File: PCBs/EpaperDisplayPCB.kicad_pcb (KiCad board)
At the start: 2 copper layers, 84 x 40.1 mm, 21 parts, among them J1 Conn_01x08, J2 Conn_01x12_FPC_0.5mm, Q1 AO3404A, U1 ePaper-2.1

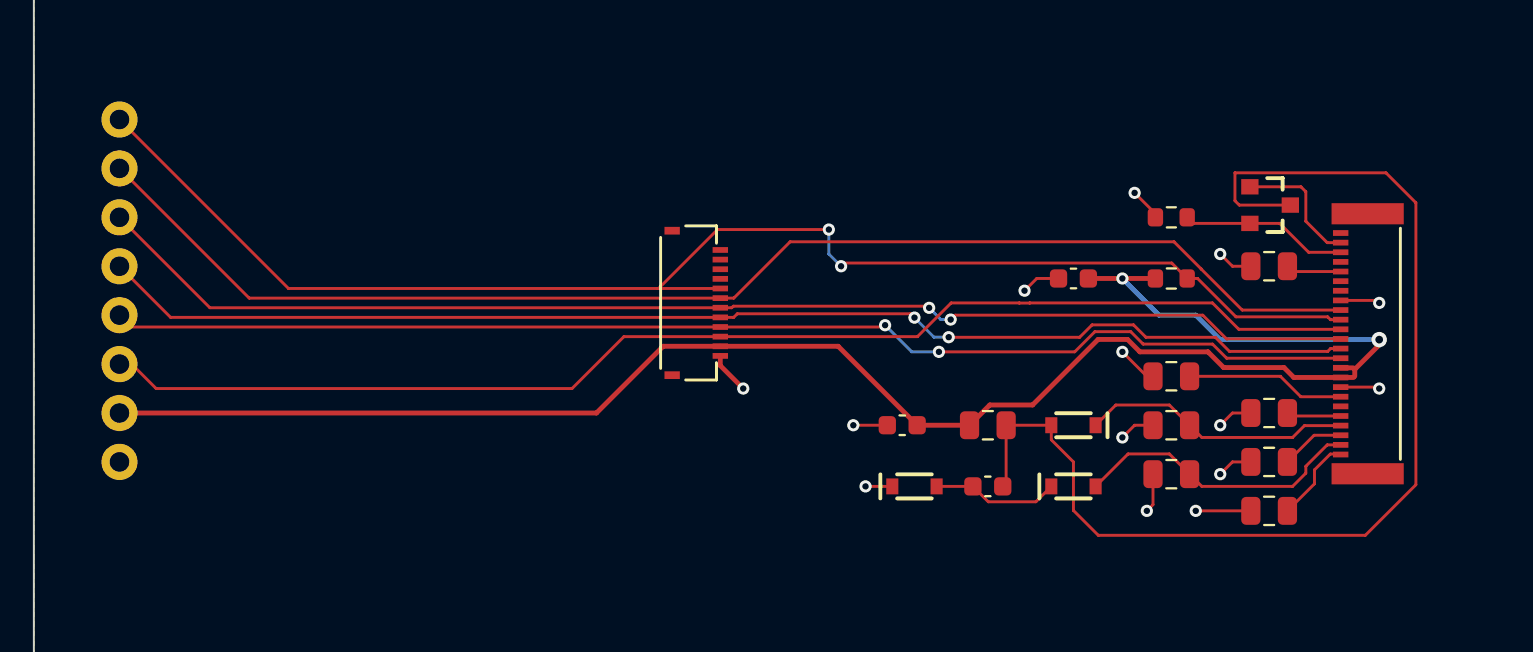
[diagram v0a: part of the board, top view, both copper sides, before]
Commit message: Updates
Fixing connections between epaper display board and main board pcbs
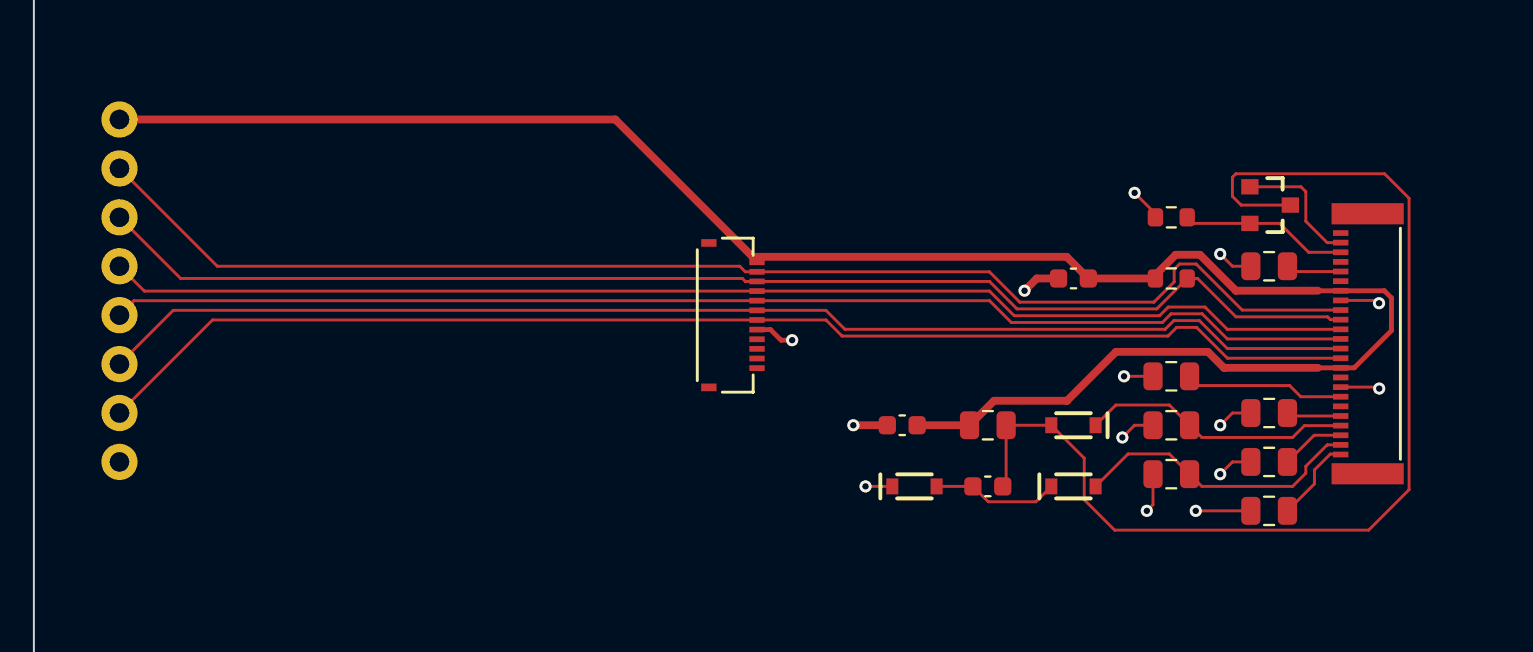
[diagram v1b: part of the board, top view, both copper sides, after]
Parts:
- removed the J2 at (152.6, 87.5)
- added J1: Conn_01x12_FPC_0.5mm, SparkFun-Connector:FPC_12_0.5MM, F.Cu at (154.6, 88.2)
- renumbered J1 to J2
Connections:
- J2 pad 1: ~{RST} -> +3.3V
- J2 pad 3: ~{CS} -> ~{RST}
- J2 pad 4: SCLK -> D/~{C}
- J2 pad 5: SDIO -> ~{CS}
- J2 pad 6: D/~{C} -> SCLK
- J2 pad 7: +3.3V -> SDIO
- U1 pad 16: +3.3V -> unconnected-(U1-NC-Pad16)
- U1 pad 7: unconnected-(U1-NC-Pad7) -> +3.3V
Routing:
- net +3.3V: track 91.3 -> 100.4 mm, vias 2 -> 0
- net ~{RST}: track 74.4 -> 66.9 mm, vias 2 -> 0
- net ~{CS}: track 66.3 -> 64.9 mm, vias 2 -> 0
- net Net-(Q1-D): track 59.0 -> 57.6 mm
- net SDIO: track 65.3 -> 66.6 mm, vias 2 -> 0
- net D/~{C}: track 66.3 -> 65.1 mm
- net GND: track 27.6 -> 26.8 mm
- net SCLK: track 66.0 -> 65.8 mm, vias 2 -> 0

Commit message: Updates
Screen PCB updates
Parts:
- added FID1: Fiducial_0.5mm, SparkFun-Aesthetic:Fiducial_0.5mm_Mask1mm, F.Cu at (122.8, 104.1)
- added FID2: Fiducial_0.5mm, SparkFun-Aesthetic:Fiducial_0.5mm_Mask1mm, F.Cu at (195.2, 72.9)
- added FID3: Fiducial_0.5mm, SparkFun-Aesthetic:Fiducial_0.5mm_Mask1mm, B.Cu at (195.2, 103.4)
- added FID4: Fiducial_0.5mm, SparkFun-Aesthetic:Fiducial_0.5mm_Mask1mm, B.Cu at (122.2, 71.0)
- added G***: LOGO, SparkFun-Aesthetic:SparkFun_Logo_NoFlame_12.5mm, F.Cu at (143.8, 100.2)
- added Ref**: Val**, SparkFun-Aesthetic:OSHW_Logo_6mm, F.Cu at (133.6, 100.2)
- added kibuzzard-65B1FFD4: G***, kibuzzard-65B1FFD4, F.Cu at (120.1, 78.1)
- added kibuzzard-65B1FFE5: G***, kibuzzard-65B1FFE5, F.Cu at (120.3, 80.6)
- added kibuzzard-65B20022: G***, kibuzzard-65B20022, F.Cu at (120.3, 83.1)
- added kibuzzard-65B20037: G***, kibuzzard-65B20037, F.Cu at (120.3, 85.6)
- added kibuzzard-65B20040: G***, kibuzzard-65B20040, F.Cu at (120.3, 88.2)
- added kibuzzard-65B2004E: G***, kibuzzard-65B2004E, F.Cu at (120.3, 90.7)
- added kibuzzard-65B2005D: G***, kibuzzard-65B2005D, F.Cu at (120.3, 93.3)
- added kibuzzard-65B2006B: G***, kibuzzard-65B2006B, F.Cu at (120.3, 95.8)
- added kibuzzard-65B200B7: G***, kibuzzard-65B200B7, F.Cu at (195.2, 97.1)
- added kibuzzard-65B200B7: G***, kibuzzard-65B200B7, F.Cu at (195.2, 82.5)
- added kibuzzard-65B200D7: G***, kibuzzard-65B200D7, F.Cu at (154.6, 93.3)
- added kibuzzard-65B20298: G***, kibuzzard-65B20298, F.Cu at (161.5, 74.2)
- U1: value ePaper-2.1 -> ePaper-2.13

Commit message: Updated Epaper Display
Updated Epaper Display with new schematic symbol and placed the correct footprint onto the PCB
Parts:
- U1: value ePaper-2.13 -> ePaper-2.66; footprint SparkFun-Display:ePaper-2.13 -> SparkFun-Display:ePaper-2.66

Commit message: epaper update
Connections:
- U1 pad 16: unconnected-(U1-NC-Pad16) -> +3.3V
- U1 pad 7: +3.3V -> unconnected-(U1-NC-Pad7)
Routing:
- net +3.3V: track 100.4 -> 100.8 mm, vias 0 -> 2

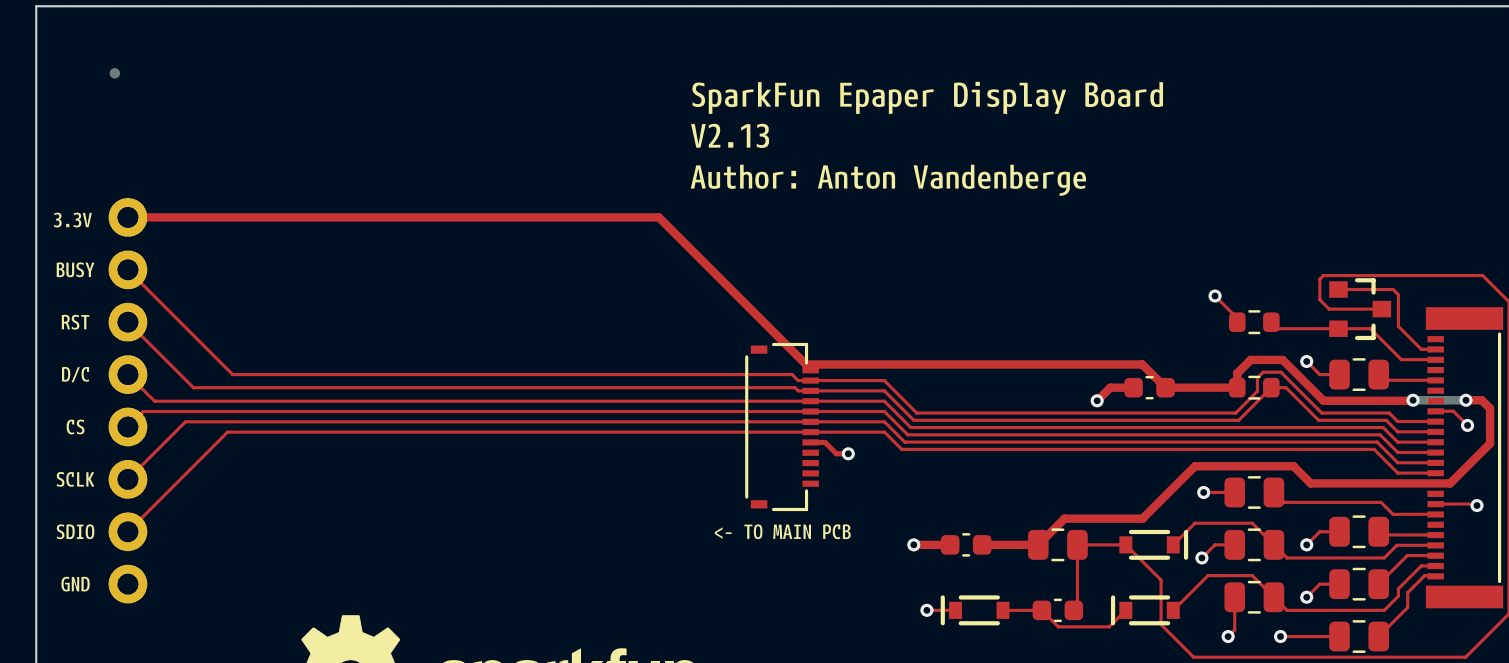
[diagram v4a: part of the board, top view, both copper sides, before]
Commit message: Current PCB updates
Updated Main Board MQ sensors and external reset button position as well as SEN 55 connector pinout.
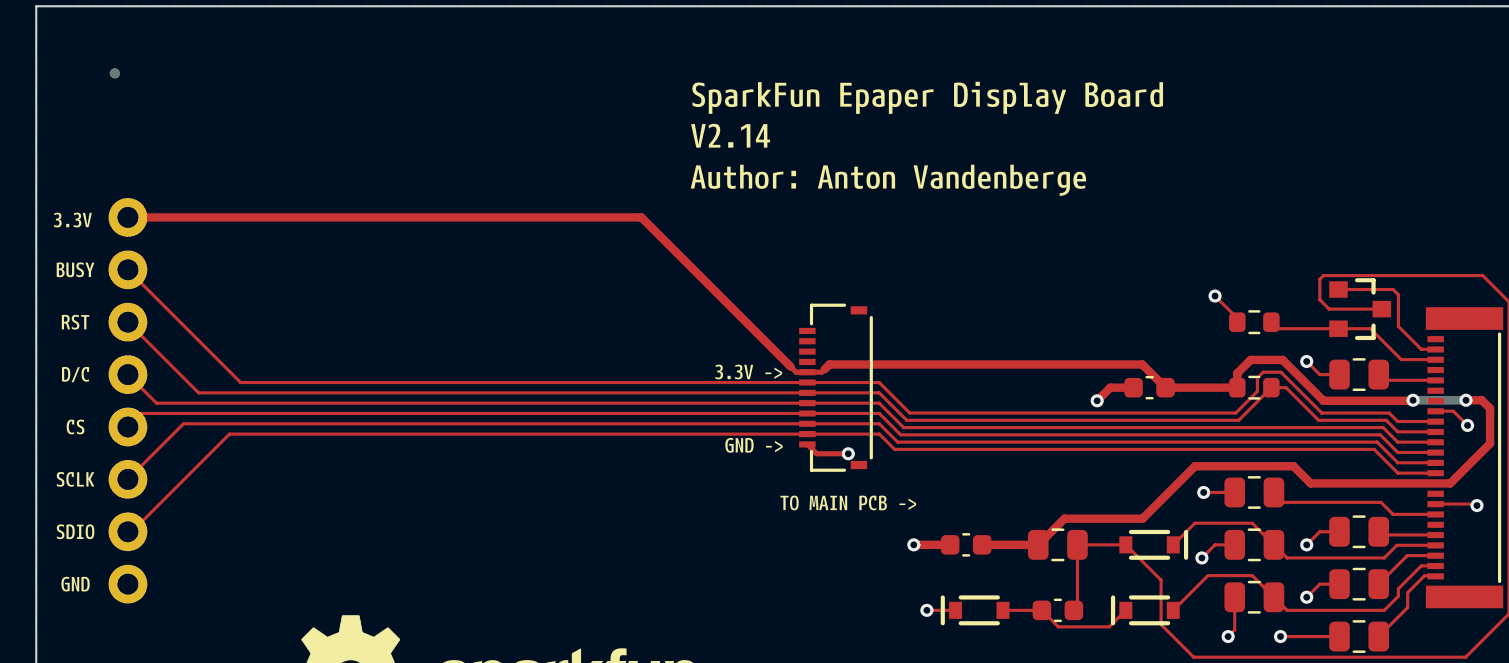
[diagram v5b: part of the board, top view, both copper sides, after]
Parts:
- removed kibuzzard-65B200D7: G***, kibuzzard-65B200D7
- removed kibuzzard-65B20298: G***, kibuzzard-65B20298
- added kibuzzard-65E12FFB: G***, kibuzzard-65E12FFB, F.Cu at (161.5, 74.2)
- added kibuzzard-65E13155: G***, kibuzzard-65E13155, F.Cu at (157.7, 91.9)
- added kibuzzard-65E131AD: G***, kibuzzard-65E131AD, F.Cu at (153.2, 89.1)
- added kibuzzard-65E131D6: G***, kibuzzard-65E131D6, F.Cu at (152.9, 85.5)
- moved J1 3.17 mm to (157.1, 86.3), turned to 90 degrees
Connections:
- J1 pad 1: +3.3V -> GND
- J1 pad 2: ~{BUSY} -> SDIO
- J1 pad 3: ~{RST} -> SCLK
- J1 pad 4: D/~{C} -> ~{CS}
- J1 pad 5: ~{CS} -> D/~{C}
- J1 pad 6: SCLK -> ~{RST}
- J1 pad 7: SDIO -> ~{BUSY}
- J1 pad 8: GND -> +3.3V

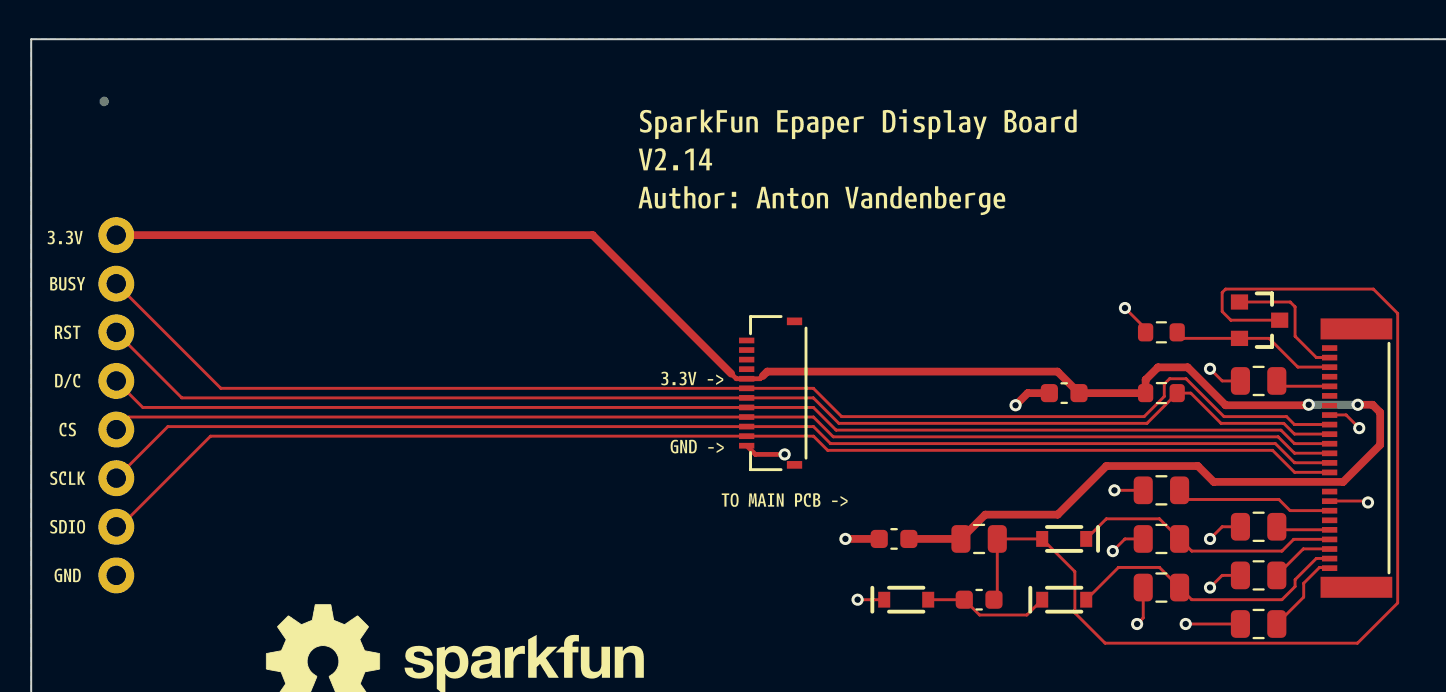
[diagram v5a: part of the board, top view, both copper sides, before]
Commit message: Screen and Main Board Updates
Updated Main board to Screen PCB connection, added accelerometer to Epaper display PCB. Removed GPIO 0 PB and replaced external Reset button with GPIO0 button.
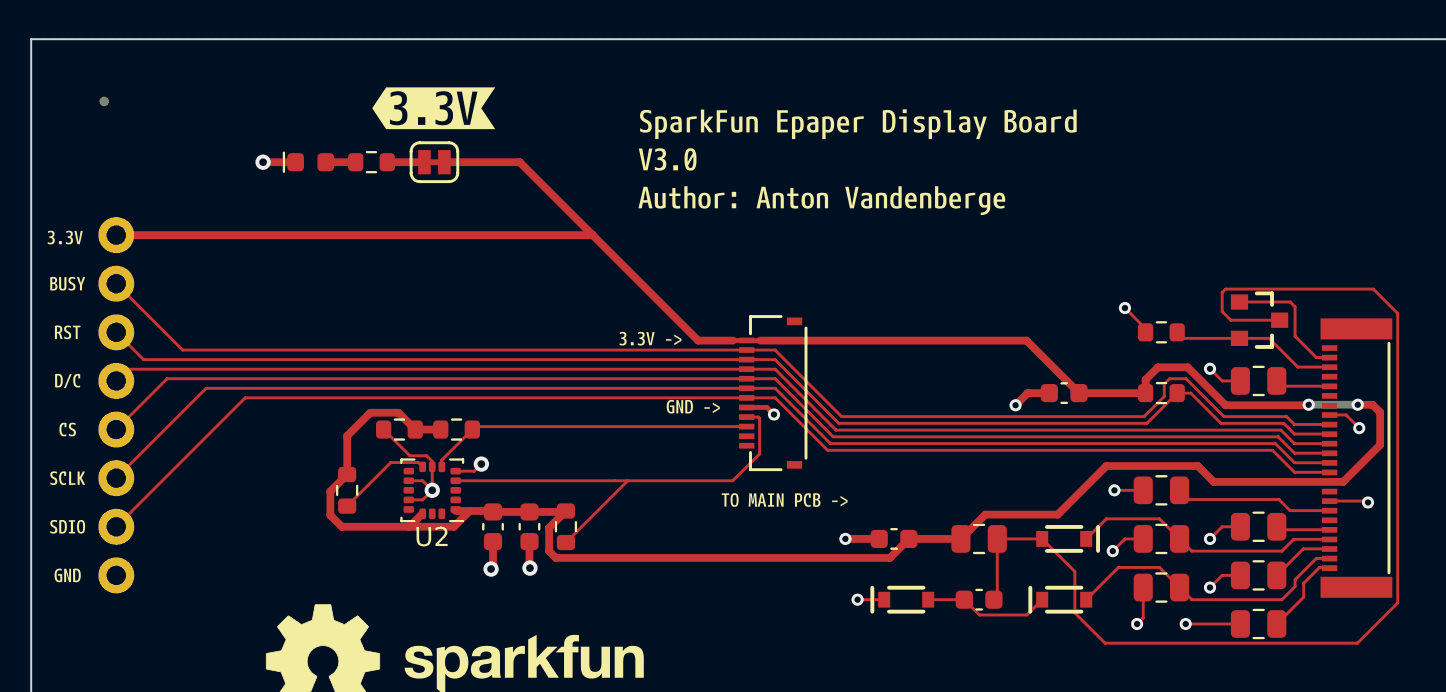
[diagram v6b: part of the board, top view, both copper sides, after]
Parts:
- removed kibuzzard-65E12FFB: G***, kibuzzard-65E12FFB
- added C11: 0.1uF, SparkFun-Capacitor:C_0603_1608Metric, F.Cu at (142.5, 93.3)
- added C12: 10uF, SparkFun-Capacitor:C_0603_1608Metric, F.Cu at (144.4, 93.3)
- added D4: Red, SparkFun-LED:LED_0603_1608Metric, F.Cu at (133.0, 74.2)
- added JP1: ~, SparkFun-Jumper:SMT-JUMPER_2_NC_TRACE_SILK, F.Cu at (139.4, 74.2)
- added R3: 10k, SparkFun-Resistor:R_0603_1608Metric, F.Cu at (136.1, 74.2)
- added R4: 10k, SparkFun-Resistor:R_0603_1608Metric, F.Cu at (134.9, 91.4)
- added R5: 4.7k, SparkFun-Resistor:R_0603_1608Metric, F.Cu at (146.3, 93.3)
- added R6: 4.7k, SparkFun-Resistor:R_0603_1608Metric, F.Cu at (140.6, 88.2)
- added R7: 10k, SparkFun-Resistor:R_0603_1608Metric, F.Cu at (137.6, 88.2)
- added U2: LIS3DH, Package_LGA:LGA-16_3x3mm_P0.5mm_LayoutBorder3x5y, F.Cu at (139.3, 91.4)
- added kibuzzard-65ECA227: G***, kibuzzard-65ECA227, F.Cu at (139.4, 71.4)
- added kibuzzard-65EF974B: G***, kibuzzard-65EF974B, F.Cu at (161.5, 74.2)
- moved kibuzzard-65E131D6 3.02 mm to (150.7, 83.4)
- moved kibuzzard-65E131AD 2.09 mm to (153.0, 87.0)
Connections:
- J1 pad 1: GND -> unconnected-(J1-Pin_1-Pad1)
- J1 pad 10: unconnected-(J1-Pin_10-Pad10) -> ~{RST}
- J1 pad 11: unconnected-(J1-Pin_11-Pad11) -> ~{BUSY}
- J1 pad 12: unconnected-(J1-Pin_12-Pad12) -> +3.3V
- J1 pad 2: SDIO -> unconnected-(J1-Pin_2-Pad2)
- J1 pad 3: SCLK -> SDA
- J1 pad 4: ~{CS} -> SCL
- J1 pad 5: D/~{C} -> GND
- J1 pad 6: ~{RST} -> SDIO
- J1 pad 7: ~{BUSY} -> SCLK
- J1 pad 8: +3.3V -> ~{CS}
- J1 pad 9: unconnected-(J1-Pin_9-Pad9) -> D/~{C}
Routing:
- net +3.3V: track 100.8 -> 156.5 mm
- net SCL: track 0.00 -> 23.6 mm
- net SDA: track 0.00 -> 17.0 mm
- net GND: track 26.7 -> 39.8 mm, vias 14 -> 19
- net Net-(U2-CS): track 0.00 -> 4.98 mm
- net Net-(JP1-A): track 0.00 -> 1.94 mm
- net SDIO: track 66.1 -> 68.0 mm
- net ~{CS}: track 64.5 -> 66.1 mm
- net SCLK: track 65.3 -> 67.0 mm
- net Net-(D4-A): track 0.00 -> 1.56 mm
- net D/~{C}: track 64.8 -> 65.3 mm
